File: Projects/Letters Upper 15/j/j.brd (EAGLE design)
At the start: 16.5 x 21.6 mm, 42 parts

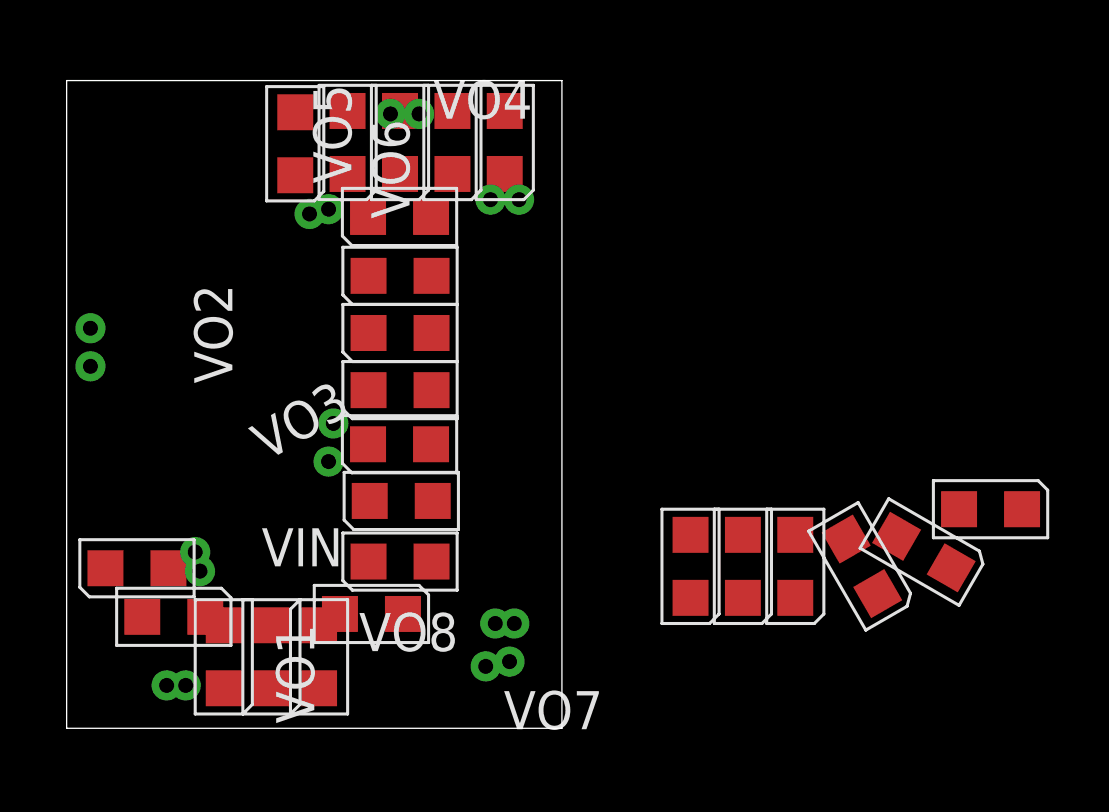
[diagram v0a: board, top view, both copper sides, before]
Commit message: 
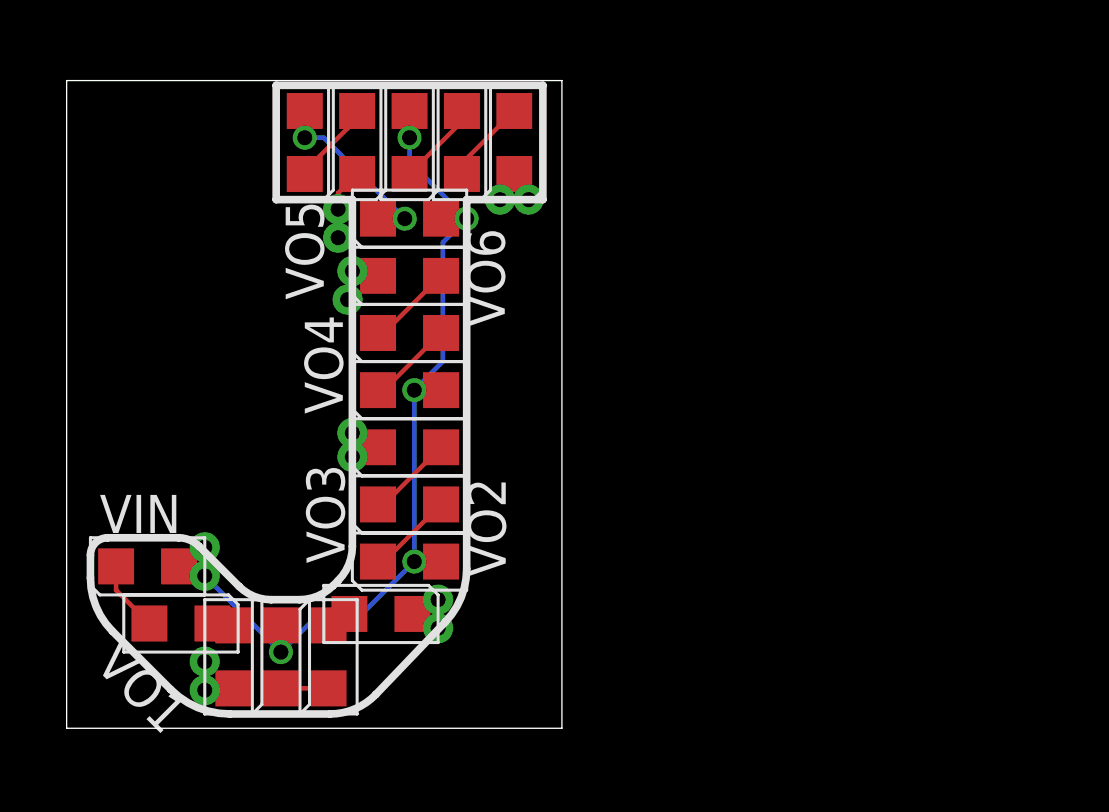
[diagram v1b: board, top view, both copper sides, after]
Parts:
- removed LED19, LED20, LED21, LED22, LED23, LED24: (no value), CyberRailGuru:LED_0805
- removed VO13, VO14, VO15, VO16: (no value), CyberRailGuru:P1-20
- moved VO2 14.0 mm to (12.4, 4.29)
- moved VO7 10.2 mm to (4.60, 1.27)
- moved VO9 10.1 mm to (9.53, 9.84)
- moved VO10 8.94 mm to (9.53, 15.2)
- moved VO4 6.63 mm to (9.37, 14.3)
- moved VO11 6.19 mm to (9.05, 16.4)
- moved VO12 4.64 mm to (14.4, 17.6)
- moved VO8 2.54 mm to (12.4, 3.33)
- moved VO1 1.50 mm to (4.60, 2.22)
- moved VO3 0.81 mm to (9.53, 9.05)
- moved LED1 0.36 mm to (2.70, 5.40)
- moved VIN 0.35 mm to (4.60, 6.03)
- moved LED9 0.35 mm to (11.4, 9.37)
- moved LED13 0.34 mm to (11.4, 17.0)
- moved LED2 0.33 mm to (3.81, 3.49)
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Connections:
- removed net N$1: LED22.C, LED23.A
- removed net N$2: LED23.C, LED24.A
- removed net N$27: LED20.C, LED21.A
- removed net N$28: LED19.C, LED20.A
- removed net N$5: LED24.C, VO16.TP, VO8.TP
- removed net VOUT7: LED21.C, VO15.TP, VO7.TP
- net VIN: no longer LED19.A, LED22.A
- net VOUT1: now also VO7.TP; no longer VO9.TP
- net VOUT2: now also VO8.TP; no longer VO10.TP
- net VOUT3: now also VO9.TP; no longer VO11.TP
- net VOUT4: now also VO10.TP; no longer VO12.TP
- net VOUT5: now also VO11.TP; no longer VO13.TP
- net VOUT6: now also VO12.TP; no longer VO14.TP
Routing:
- net VIN: track 0.00 -> 31.5 mm, vias 0 -> 5
- net N$20: track 0.00 -> 6.23 mm, vias 0 -> 2
- net N$24: track 0.00 -> 3.18 mm
- net N$19: track 0.00 -> 2.97 mm
- net N$15: track 0.00 -> 2.89 mm
- net N$11: track 0.00 -> 2.89 mm
- net N$16: track 0.00 -> 2.89 mm
- net N$12: track 0.00 -> 2.89 mm
- net N$23: track 0.00 -> 2.82 mm
- net VOUT5: track 0.00 -> 2.39 mm
- net N$4: track 0.00 -> 2.37 mm
- net VOUT6: track 0.00 -> 2.10 mm
- net VOUT2: track 0.00 -> 2.10 mm
- net VOUT3: track 0.00 -> 2.04 mm
- net VOUT4: track 0.00 -> 1.94 mm
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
